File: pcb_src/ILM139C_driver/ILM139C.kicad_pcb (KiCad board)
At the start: 4 copper layers, 26 x 18 mm, 64 parts, among them CN1 HC-1.0-2PWT, CN2 HC-1.0-2PWT, CN5 AXE540127D, CN6 AXE540127D, U1 IS31FL3741A-QFLS4-TR, U2 HC-1.0-4PWT-B-HW, U3 HC-1.0-4PWT-B-HW

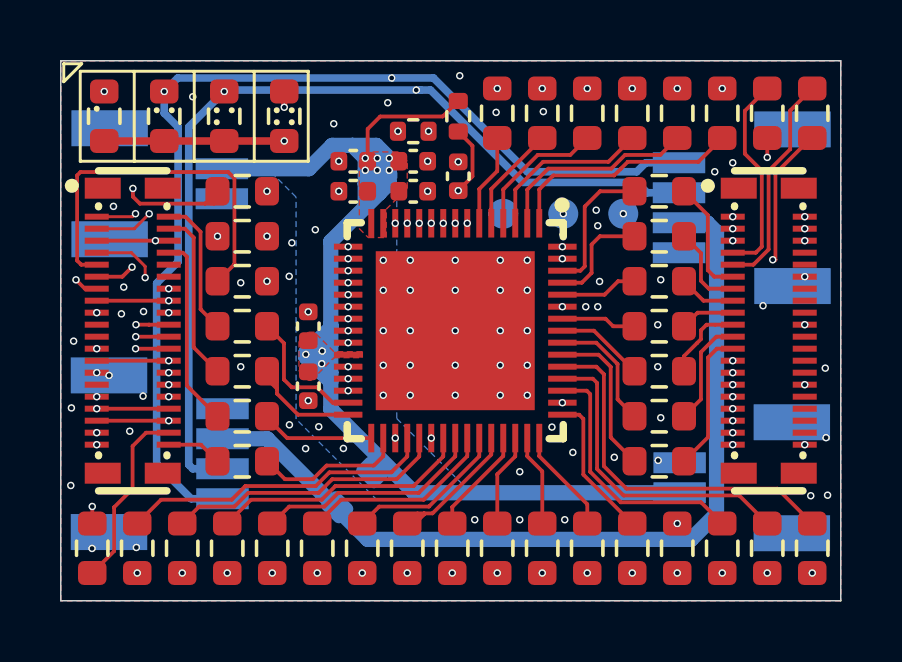
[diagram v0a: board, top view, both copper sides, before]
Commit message: Added pinout, fixed qwiic
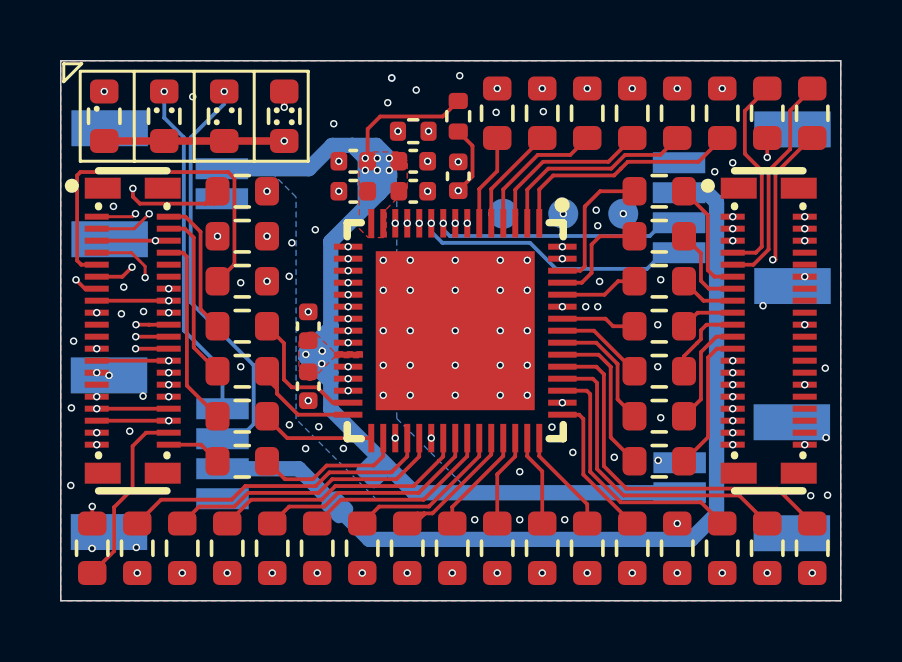
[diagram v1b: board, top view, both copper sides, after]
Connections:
- U2 pad 1: SCL -> GND
- U2 pad 2: SDA -> 3V3
- U2 pad 3: 3V3 -> SDA
- U2 pad 4: GND -> SCL
- U3 pad 1: SCL -> GND
- U3 pad 2: SDA -> 3V3
- U3 pad 3: 3V3 -> SDA
- U3 pad 4: GND -> SCL
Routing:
- net SCL: track 53.2 -> 39.5 mm
- net SDA: track 47.1 -> 38.5 mm
- net 3V3: track 29.0 -> 29.6 mm
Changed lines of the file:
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@@
 		(sheetname "/")
 		(sheetfile "ILM139C.kicad_sch")
-		(attr smd dnp)
+		(attr smd)
 		(fp_line
 			(start -0.237258 -0.5225)
@@
 		(sheetname "/")
 		(sheetfile "ILM139C.kicad_sch")
-		(attr smd dnp)
+		(attr smd)
 		(fp_line
 			(start -0.237258 -0.5225)
@@
 		(sheetname "/")
 		(sheetfile "ILM139C.kicad_sch")
-		(attr smd dnp)
+		(attr smd)
 		(fp_line
 			(start -0.237258 -0.5225)
@@
 			(layer "B.Fab")
 		)
-		(fp_text user "${REFERENCE}"
-			(at 0 0 90)
-			(layer "B.Fab")
-			(effects
-				(font
-					(size 1 1)
-					(thickness 0.15)
-				)
-				(justify mirror)
-			)
-		)
 		(pad "1" smd rect
 			(at -1.5 1.89 270)
 			(size 0.7 1.75)
 			(layers "B.Cu" "B.Mask" "B.Paste")
-			(net 1 "SCL")
+			(net 2 "GND")
 			(pinfunction "1")
 			(pintype "unspecified")
@@
 			(size 0.7 1.75)
 			(layers "B.Cu" "B.Mask" "B.Paste")
-			(net 3 "SDA")
+			(net 104 "3V3")
 			(pinfunction "2")
 			(pintype "unspecified")
@@
 			(size 0.7 1.75)
 			(layers "B.Cu" "B.Mask" "B.Paste")
-			(net 104 "3V3")
+			(net 3 "SDA")
 			(pinfunction "3")
 			(pintype "unspecified")
@@
 			(size 0.7 1.75)
 			(layers "B.Cu" "B.Mask" "B.Paste")
-			(net 2 "GND")
+			(net 1 "SCL")
 			(pinfunction "4")
 			(pintype "unspecified")
@@
 			(layer "B.Fab")
 		)
-		(fp_text user "${REFERENCE}"
-			(at 0 0 270)
-			(layer "B.Fab")
-			(effects
-				(font
-					(size 1 1)
-					(thickness 0.15)
-				)
-				(justify mirror)
-			)
-		)
 		(pad "1" smd rect
 			(at -1.5 1.89 90)
 			(size 0.7 1.75)
 			(layers "B.Cu" "B.Mask" "B.Paste")
-			(net 1 "SCL")
+			(net 2 "GND")
 			(pinfunction "1")
 			(pintype "unspecified")
@@
 			(size 0.7 1.75)
 			(layers "B.Cu" "B.Mask" "B.Paste")
-			(net 3 "SDA")
+			(net 104 "3V3")
 			(pinfunction "2")
 			(pintype "unspecified")
@@
 			(size 0.7 1.75)
 			(layers "B.Cu" "B.Mask" "B.Paste")
-			(net 104 "3V3")
+			(net 3 "SDA")
 			(pinfunction "3")
 			(pintype "unspecified")
@@
 			(size 0.7 1.75)
 			(layers "B.Cu" "B.Mask" "B.Paste")
-			(net 2 "GND")
+			(net 1 "SCL")
 			(pinfunction "4")
 			(pintype "unspecified")
@@
 	)
 	(segment
-		(start 105.5 55.558501)
-		(end 109.15 55.558501)
-		(width 0.254)
-		(layer "B.Cu")
-		(net 1)
-	)
-	(segment
-		(start 93.862 54.070501)
-		(end 93.4 53.608501)
-		(width 0.254)
+		(start 102.3 57.555)
+		(end 102.3 57.276501)
+		(width 0.127)
 		(layer "B.Cu")
 		(net 1)
 	)
 	(segment
-		(start 94.3 66.458501)
-		(end 93.147 65.305501)
-		(width 0.254)
+		(start 94.0525 54.4145)
+		(end 93.4 53.762)
+		(width 0.127)
 		(layer "B.Cu")
 		(net 1)
 	)
 	(segment
-		(start 102.374 52.432501)
-		(end 105.5 55.558501)
-		(width 0.254)
+		(start 106.460001 58.796001)
+		(end 105.592 57.928)
+		(width 0.127)
 		(layer "B.Cu")
 		(net 1)
 	)
 	(segment
-		(start 100.984 52.431501)
-		(end 100.985 52.432501)
-		(width 0.254)
+		(start 110.025499 58.262501)
+		(end 109.491999 58.796001)
+		(width 0.127)
 		(layer "B.Cu")
 		(net 1)
 	)
 	(segment
-		(start 100.982 52.433501)
-		(end 93.85 52.433501)
-		(width 0.254)
+		(start 109.491999 58.796001)
+		(end 106.460001 58.796001)
+		(width 0.127)
 		(layer "B.Cu")
 		(net 1)
 	)
 	(segment
-		(start 93.862 58.558501)
-		(end 93.862 54.070501)
-		(width 0.254)
+		(start 95.34 62.135)
+		(end 94.0525 60.8475)
+		(width 0.127)
 		(layer "B.Cu")
 		(net 1)
 	)
 	(segment
-		(start 93.85 52.433501)
-		(end 93.4 52.883501)
+		(start 100.984 52.431501)
+		(end 100.985 52.432501)
 		(width 0.254)
 		(layer "B.Cu")
@@
 	)
 	(segment
-		(start 109.45 55.258501)
-		(end 110.56 55.258501)
-		(width 0.254)
+		(start 110.025499 58.258501)
+		(end 110.025499 58.262501)
+		(width 0.127)
 		(layer "B.Cu")
 		(net 1)
 	)
 	(segment
-		(start 93.4 53.608501)
+		(start 93.4 53.762)
 		(end 93.4 52.883501)
-		(width 0.254)
+		(width 0.127)
 		(layer "B.Cu")
 		(net 1)
 	)
 	(segment
-		(start 93.147 65.305501)
-		(end 93.147 59.273501)
+		(start 100.984 52.431501)
+		(end 100.982 52.433501)
 		(width 0.254)
 		(layer "B.Cu")
@@
 	)
 	(segment
-		(start 93.147 59.273501)
-		(end 93.862 58.558501)
-		(width 0.254)
+		(start 95.34 63.458501)
+		(end 95.34 62.135)
+		(width 0.127)
 		(layer "B.Cu")
 		(net 1)
 	)
 	(segment
-		(start 100.984 52.431501)
-		(end 100.982 52.433501)
-		(width 0.254)
+		(start 102.673 57.928)
+		(end 102.3 57.555)
+		(width 0.127)
 		(layer "B.Cu")
 		(net 1)
 	)
 	(segment
-		(start 95.34 66.458501)
-		(end 94.3 66.458501)
-		(width 0.254)
+		(start 94.0525 60.8475)
+		(end 94.0525 54.4145)
+		(width 0.127)
 		(layer "B.Cu")
 		(net 1)
 	)
 	(segment
-		(start 100.985 52.432501)
-		(end 102.374 52.432501)
-		(width 0.254)
+		(start 110.56 58.258501)
+		(end 110.025499 58.258501)
+		(width 0.127)
 		(layer "B.Cu")
 		(net 1)
 	)
 	(segment
-		(start 109.15 55.558501)
-		(end 109.45 55.258501)
-		(width 0.254)
+		(start 105.592 57.928)
+		(end 102.673 57.928)
+		(width 0.127)
 		(layer "B.Cu")
 		(net 1)
@@
 	)
 	(segment
-		(start 105.352954 55.913501)
-		(end 109.155 55.913501)
-		(width 0.254)
+		(start 95.4 53.298)
+		(end 94.2805 54.4175)
+		(width 0.127)
 		(layer "B.Cu")
 		(net 3)
 	)
 	(segment
-		(start 101.942 52.835501)
-		(end 102.274954 52.835501)
-		(width 0.254)
+		(start 102.7 57.481)
+		(end 102.919 57.7)
+		(width 0.127)
 		(layer "B.Cu")
 		(net 3)
 	)
 	(segment
-		(start 109.155 55.913501)
-		(end 109.5 56.258501)
-		(width 0.254)
+		(start 102.7 57.276501)
+		(end 102.7 57.481)
+		(width 0.127)
 		(layer "B.Cu")
 		(net 3)
 	)
 	(segment
-		(start 94.217 65.325501)
-		(end 94.217 54.066501)
-		(width 0.254)
+		(start 109.586 57.7)
+		(end 110.027499 57.258501)
+		(width 0.127)
 		(layer "B.Cu")
 		(net 3)
 	)
 	(segment
-		(start 101.942 52.835501)
-		(end 95.448 52.835501)
-		(width 0.254)
+		(start 101.799 52.835501)
+		(end 101.799 52.770375)
+		(width 0.127)
 		(layer "B.Cu")
 		(net 3)
 	)
 	(segment
-		(start 109.5 56.258501)
-		(end 110.56 56.258501)
-		(width 0.254)
+		(start 94.2805 54.4175)
+		(end 94.2805 59.908875)
+		(width 0.127)
 		(layer "B.Cu")
 		(net 3)
 	)
 	(segment
-		(start 94.35 65.458501)
-		(end 94.217 65.325501)
-		(width 0.254)
+		(start 95.4 52.883501)
+		(end 95.4 53.298)
+		(width 0.127)
 		(layer "B.Cu")
 		(net 3)
 	)
 	(segment
-		(start 94.217 54.066501)
-		(end 95.4 52.883501)
-		(width 0.254)
+		(start 95.894 64.458501)
+		(end 95.34 64.458501)
+		(width 0.127)
 		(layer "B.Cu")
 		(net 3)
 	)
 	(segment
-		(start 102.274954 52.835501)
-		(end 105.352954 55.913501)
-		(width 0.254)
+		(start 96.3795 62.007875)
+		(end 96.3795 63.973001)
+		(width 0.127)
 		(layer "B.Cu")
 		(net 3)
 	)
 	(segment
-		(start 95.448 52.835501)
-		(end 95.4 52.883501)
-		(width 0.254)
+		(start 96.3795 63.973001)
+		(end 95.894 64.458501)
+		(width 0.127)
 		(layer "B.Cu")
 		(net 3)
 	)
 	(segment
-		(start 95.34 65.458501)
-		(end 94.35 65.458501)
-		(width 0.254)
+		(start 110.027499 57.258501)
+		(end 110.56 57.258501)
+		(width 0.127)
+		(layer "B.Cu")
+		(net 3)
+	)
+	(segment
+		(start 102.919 57.7)
+		(end 109.586 57.7)
+		(width 0.127)
+		(layer "B.Cu")
+		(net 3)
+	)
+	(segment
+		(start 95.4 52.883501)
+		(end 95.4 52.865)
+		(width 0.127)
+		(layer "B.Cu")
+		(net 3)
+	)
+	(segment
+		(start 94.2805 59.908875)
+		(end 96.3795 62.007875)
+		(width 0.127)
 		(layer "B.Cu")
 		(net 3)
@@
 	)
 	(segment
-		(start 111.495 57.258501)
-		(end 110.56 57.258501)
+		(start 97.883274 65.458501)
+		(end 95.34 65.458501)
 		(width 0.508)
 		(layer "B.Cu")
@@
 	)
 	(segment
-		(start 95.34 64.458501)
-		(end 96.83 64.458501)
+		(start 99.166637 66.741864)
+		(end 100.238274 67.813501)
 		(width 0.508)
 		(layer "B.Cu")
@@
 	)
 	(segment
-		(start 111.81 66.963501)
-		(end 111.81 57.573501)
+		(start 110.96 67.813501)
+		(end 111.81 66.963501)
 		(width 0.508)
 		(layer "B.Cu")
@@
 	)
 	(segment
-		(start 110.96 67.813501)
-		(end 111.81 66.963501)
+		(start 111.495 56.258501)
+		(end 110.56 56.258501)
 		(width 0.508)
 		(layer "B.Cu")
@@
 	)
 	(segment
-		(start 100.185 67.813501)
+		(start 100.238274 67.813501)
 		(end 110.96 67.813501)
 		(width 0.508)
@@
 	)
 	(segment
-		(start 96.83 64.458501)
-		(end 100.185 67.813501)
+		(start 111.81 66.963501)
+		(end 111.81 56.573501)
+		(width 0.508)
+		(layer "B.Cu")
+		(net 104)
+	)
+	(segment
+		(start 111.81 56.573501)
+		(end 111.495 56.258501)
 		(width 0.508)
 		(layer "B.Cu")
@@
 	)
 	(segment
-		(start 111.81 57.573501)
-		(end 111.495 57.258501)
+		(start 99.166637 66.741864)
+		(end 97.883274 65.458501)
 		(width 0.508)
 		(layer "B.Cu")

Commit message: Added production files
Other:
- board text added: "⠁ 0x00 ⠉ 0x01 ⠋ 0x10 ⠛ 0x11"
- board text removed: "⠁ 0x00 ⠉ 0x00 ⠋ 0x00 ⠛ 0x00"
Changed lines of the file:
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@@
 			(drillshape 0)
 			(scaleselection 1)
-			(outputdirectory "Gerbers/")
+			(outputdirectory "./production")
 		)
 	)
@@
 		)
 	)
-	(gr_text "⠁ 0x00\n⠉ 0x00\n⠋ 0x00\n⠛ 0x00\n"
+	(gr_text "⠁ 0x00\n⠉ 0x01\n⠋ 0x10\n⠛ 0x11\n"
 		(at 99.85 55.358501 0)
 		(layer "B.SilkS")
@@
 			(justify mirror)
 		)
-		(render_cache "⠁ 0x00\n⠉ 0x00\n⠋ 0x00\n⠛ 0x00\n" 0
+		(render_cache "⠁ 0x00\n⠉ 0x01\n⠋ 0x10\n⠛ 0x11\n" 0
 			(polygon
 				(pts
@@
 			(polygon
 				(pts
-					(xy 98.141916 54.191718) (xy 98.197636 54.20546) (xy 98.24629 54.227509) (xy 98.288976 54.257857)
-					(xy 98.326412 54.297105) (xy 98.355988 54.34146) (xy 98.379991 54.393665) (xy 98.398118 54.45495)
-					(xy 98.409723 54.526778) (xy 98.413851 54.61081) (xy 98.409728 54.694569) (xy 98.398132 54.766216)
-					(xy 98.380012 54.827398) (xy 98.356006 54.879563) (xy 98.326412 54.92393) (xy 98.288976 54.963178)
-					(xy 98.24629 54.993526) (xy 98.197636 55.015574) (xy 98.141916 55.029316) (xy 98.077724 55.034132)
-					(xy 98.013797 55.029323) (xy 97.958256 55.015596) (xy 97.909708 54.993557) (xy 97.867067 54.963205)
-					(xy 97.829622 54.92393) (xy 97.800029 54.879563) (xy 97.776023 54.827398) (xy 97.757903 54.766216)
-					(xy 97.746307 54.694569) (xy 97.742183 54.61081) (xy 97.742279 54.608856) (xy 97.952574 54.608856)
-					(xy 97.956762 54.713275) (xy 97.967278 54.78291) (xy 97.981541 54.826916) (xy 97.998984 54.855352)
-					(xy 98.020319 54.874633) (xy 98.046099 54.886246) (xy 98.077724 54.890322) (xy 98.109636 54.886232)
-					(xy 98.135586 54.874598) (xy 98.156999 54.855313) (xy 98.174444 54.826916) (xy 98.188708 54.78291)
-					(xy 98.199223 54.713275) (xy 98.203412 54.608856) (xy 98.199222 54.505568) (xy 98.188707 54.436744)
-					(xy 98.174444 54.393288) (xy 98.157047 54.365321) (xy 98.135661 54.346279) (xy 98.109696 54.334765)
-					(xy 98.077724 54.330713) (xy 98.045757 54.334769) (xy 98.019849 54.346287) (xy 97.998559 54.365326)
-					(xy 97.981297 54.393288) (xy 97.967158 54.436732) (xy 97.956729 54.505556) (xy 97.952574 54.608856)
-					(xy 97.742279 54.608856) (xy 97.746312 54.526778) (xy 97.757917 54.45495) (xy 97.776044 54.393665)
-					(xy 97.800047 54.34146) (xy 97.829622 54.297105) (xy 97.867067 54.25783) (xy 97.909708 54.227478)
-					(xy 97.958256 54.205439) (xy 98.013797 54.191711) (xy 98.077724 54.186902)
+					(xy 98.336231 54.871564) (xy 98.150411 54.871564) (xy 98.150411 54.346344) (xy 98.341165 54.386986)
+					(xy 98.341165 54.243176) (xy 98.151534 54.202534) (xy 97.9515 54.202534) (xy 97.9515 54.871564)
+					(xy 97.76568 54.871564) (xy 97.76568 55.018501) (xy 98.336231 55.018501)
 				)
 			)
@@
 			(polygon
 				(pts
-					(xy 98.921148 55.535718) (xy 98.976868 55.54946) (xy 99.025522 55.571509) (xy 99.068208 55.601857)
-					(xy 99.105645 55.641105) (xy 99.13522 55.68546) (xy 99.159224 55.737665) (xy 99.17735 55.79895)
-					(xy 99.188955 55.870778) (xy 99.193084 55.95481) (xy 99.18896 56.038569) (xy 99.177364 56.110216)
-					(xy 99.159244 56.171398) (xy 99.135238 56.223563) (xy 99.105645 56.26793) (xy 99.068208 56.307178)
-					(xy 99.025522 56.337526) (xy 98.976868 56.359574) (xy 98.921148 56.373316) (xy 98.856957 56.378132)
-					(xy 98.79303 56.373323) (xy 98.737489 56.359596) (xy 98.688941 56.337557) (xy 98.6463 56.307205)
-					(xy 98.608855 56.26793) (xy 98.579261 56.223563) (xy 98.555255 56.171398) (xy 98.537135 56.110216)
-					(xy 98.525539 56.038569) (xy 98.521416 55.95481) (xy 98.521512 55.952856) (xy 98.731807 55.952856)
-					(xy 98.735995 56.057275) (xy 98.746511 56.12691) (xy 98.760774 56.170916) (xy 98.778216 56.199352)
-					(xy 98.799551 56.218633) (xy 98.825331 56.230246) (xy 98.856957 56.234322) (xy 98.888868 56.230232)
-					(xy 98.914818 56.218598) (xy 98.936231 56.199313) (xy 98.953677 56.170916) (xy 98.96794 56.12691)
-					(xy 98.978456 56.057275) (xy 98.982644 55.952856) (xy 98.978455 55.849568) (xy 98.967939 55.780744)
-					(xy 98.953677 55.737288) (xy 98.93628 55.709321) (xy 98.914893 55.690279) (xy 98.888928 55.678765)
-					(xy 98.856957 55.674713) (xy 98.824989 55.678769) (xy 98.799081 55.690287) (xy 98.777792 55.709326)
-					(xy 98.76053 55.737288) (xy 98.74639 55.780732) (xy 98.735962 55.849556) (xy 98.731807 55.952856)
-					(xy 98.521512 55.952856) (xy 98.525544 55.870778) (xy 98.537149 55.79895) (xy 98.555276 55.737665)
-					(xy 98.579279 55.68546) (xy 98.608855 55.641105) (xy 98.6463 55.60183) (xy 98.688941 55.571478)
-					(xy 98.737489 55.549439) (xy 98.79303 55.535711) (xy 98.856957 55.530902)
+					(xy 99.115463 56.215564) (xy 98.929643 56.215564) (xy 98.929643 55.690344) (xy 99.120397 55.730986)
+					(xy 99.120397 55.587176) (xy 98.930767 55.546534) (xy 98.730732 55.546534) (xy 98.730732 56.215564)
+					(xy 98.544912 56.215564) (xy 98.544912 56.362501) (xy 99.115463 56.362501)
 				)
 			)
@@
 			(polygon
 				(pts
-					(xy 98.921148 56.879718) (xy 98.976868 56.89346) (xy 99.025522 56.915509) (xy 99.068208 56.945857)
-					(xy 99.105645 56.985105) (xy 99.13522 57.02946) (xy 99.159224 57.081665) (xy 99.17735 57.14295)
-					(xy 99.188955 57.214778) (xy 99.193084 57.29881) (xy 99.18896 57.382569) (xy 99.177364 57.454216)
-					(xy 99.159244 57.515398) (xy 99.135238 57.567563) (xy 99.105645 57.61193) (xy 99.068208 57.651178)
-					(xy 99.025522 57.681526) (xy 98.976868 57.703574) (xy 98.921148 57.717316) (xy 98.856957 57.722132)
-					(xy 98.79303 57.717323) (xy 98.737489 57.703596) (xy 98.688941 57.681557) (xy 98.6463 57.651205)
-					(xy 98.608855 57.61193) (xy 98.579261 57.567563) (xy 98.555255 57.515398) (xy 98.537135 57.454216)
-					(xy 98.525539 57.382569) (xy 98.521416 57.29881) (xy 98.521512 57.296856) (xy 98.731807 57.296856)
-					(xy 98.735995 57.401275) (xy 98.746511 57.47091) (xy 98.760774 57.514916) (xy 98.778216 57.543352)
-					(xy 98.799551 57.562633) (xy 98.825331 57.574246) (xy 98.856957 57.578322) (xy 98.888868 57.574232)
-					(xy 98.914818 57.562598) (xy 98.936231 57.543313) (xy 98.953677 57.514916) (xy 98.96794 57.47091)
-					(xy 98.978456 57.401275) (xy 98.982644 57.296856) (xy 98.978455 57.193568) (xy 98.967939 57.124744)
-					(xy 98.953677 57.081288) (xy 98.93628 57.053321) (xy 98.914893 57.034279) (xy 98.888928 57.022765)
-					(xy 98.856957 57.018713) (xy 98.824989 57.022769) (xy 98.799081 57.034287) (xy 98.777792 57.053326)
-					(xy 98.76053 57.081288) (xy 98.74639 57.124732) (xy 98.735962 57.193556) (xy 98.731807 57.296856)
-					(xy 98.521512 57.296856) (xy 98.525544 57.214778) (xy 98.537149 57.14295) (xy 98.555276 57.081665)
-					(xy 98.579279 57.02946) (xy 98.608855 56.985105) (xy 98.6463 56.94583) (xy 98.688941 56.915478)
-					(xy 98.737489 56.893439) (xy 98.79303 56.879711) (xy 98.856957 56.874902)
+					(xy 99.115463 57.559564) (xy 98.929643 57.559564) (xy 98.929643 57.034344) (xy 99.120397 57.074986)
+					(xy 99.120397 56.931176) (xy 98.930767 56.890534) (xy 98.730732 56.890534) (xy 98.730732 57.559564)
+					(xy 98.544912 57.559564) (xy 98.544912 57.706501) (xy 99.115463 57.706501)
 				)
 			)
 			(polygon
 				(pts
-					(xy 98.141916 56.879718) (xy 98.197636 56.89346) (xy 98.24629 56.915509) (xy 98.288976 56.945857)
-					(xy 98.326412 56.985105) (xy 98.355988 57.02946) (xy 98.379991 57.081665) (xy 98.398118 57.14295)
-					(xy 98.409723 57.214778) (xy 98.413851 57.29881) (xy 98.409728 57.382569) (xy 98.398132 57.454216)
-					(xy 98.380012 57.515398) (xy 98.356006 57.567563) (xy 98.326412 57.61193) (xy 98.288976 57.651178)
-					(xy 98.24629 57.681526) (xy 98.197636 57.703574) (xy 98.141916 57.717316) (xy 98.077724 57.722132)
-					(xy 98.013797 57.717323) (xy 97.958256 57.703596) (xy 97.909708 57.681557) (xy 97.867067 57.651205)
-					(xy 97.829622 57.61193) (xy 97.800029 57.567563) (xy 97.776023 57.515398) (xy 97.757903 57.454216)
-					(xy 97.746307 57.382569) (xy 97.742183 57.29881) (xy 97.742279 57.296856) (xy 97.952574 57.296856)
-					(xy 97.956762 57.401275) (xy 97.967278 57.47091) (xy 97.981541 57.514916) (xy 97.998984 57.543352)
-					(xy 98.020319 57.562633) (xy 98.046099 57.574246) (xy 98.077724 57.578322) (xy 98.109636 57.574232)
-					(xy 98.135586 57.562598) (xy 98.156999 57.543313) (xy 98.174444 57.514916) (xy 98.188708 57.47091)
-					(xy 98.199223 57.401275) (xy 98.203412 57.296856) (xy 98.199222 57.193568) (xy 98.188707 57.124744)
-					(xy 98.174444 57.081288) (xy 98.157047 57.053321) (xy 98.135661 57.034279) (xy 98.109696 57.022765)
-					(xy 98.077724 57.018713) (xy 98.045757 57.022769) (xy 98.019849 57.034287) (xy 97.998559 57.053326)
-					(xy 97.981297 57.081288) (xy 97.967158 57.124732) (xy 97.956729 57.193556) (xy 97.952574 57.296856)
-					(xy 97.742279 57.296856) (xy 97.746312 57.214778) (xy 97.757917 57.14295) (xy 97.776044 57.081665)
-					(xy 97.800047 57.02946) (xy 97.829622 56.985105) (xy 97.867067 56.94583) (xy 97.909708 56.915478)
-					(xy 97.958256 56.893439) (xy 98.013797 56.879711) (xy 98.077724 56.874902)
+					(xy 98.336231 57.559564) (xy 98.150411 57.559564) (xy 98.150411 57.034344) (xy 98.341165 57.074986)
+					(xy 98.341165 56.931176) (xy 98.151534 56.890534) (xy 97.9515 56.890534) (xy 97.9515 57.559564)
+					(xy 97.76568 57.559564) (xy 97.76568 57.706501) (xy 98.336231 57.706501)
 				)
 			)
